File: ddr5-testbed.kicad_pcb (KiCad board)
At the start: 6 copper layers, 69.6 x 30 mm, 64 parts, among them IC1 PCA6408APW, IC2 AT24CS01, J1 ddr4-sodimm-edge-connector, U1 MT60B2G8HB-48B_A, U2 TPS613221ADBVT

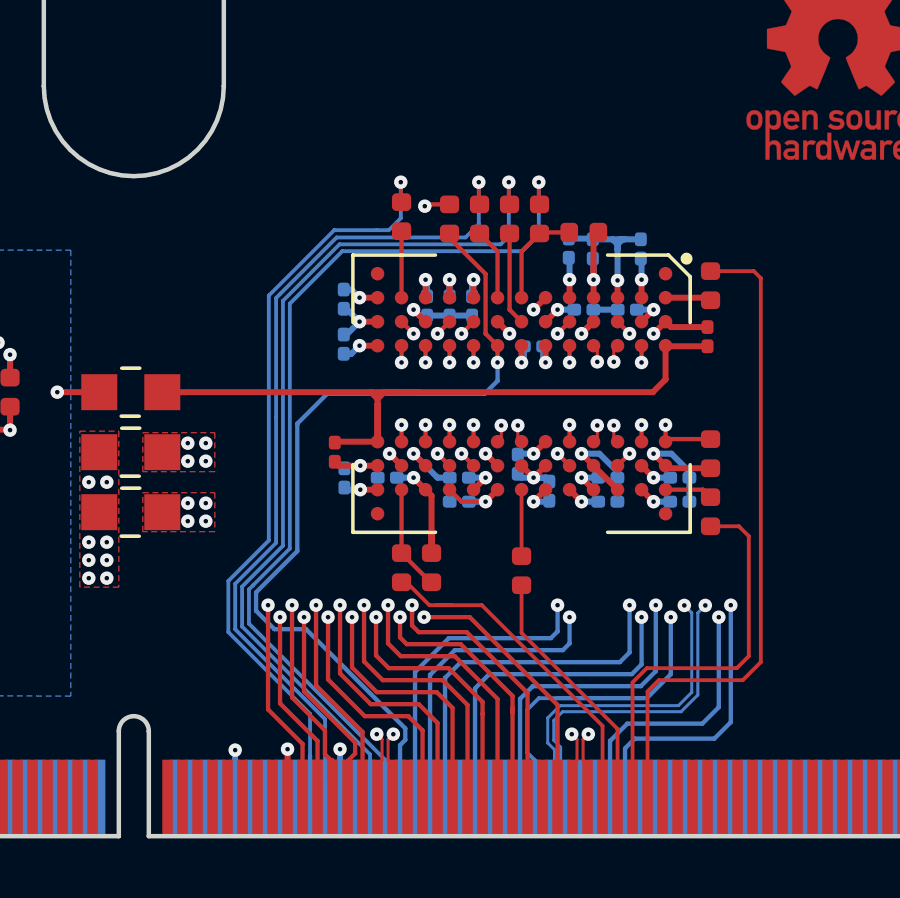
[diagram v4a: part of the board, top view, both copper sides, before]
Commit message: Finish SODIMM connections
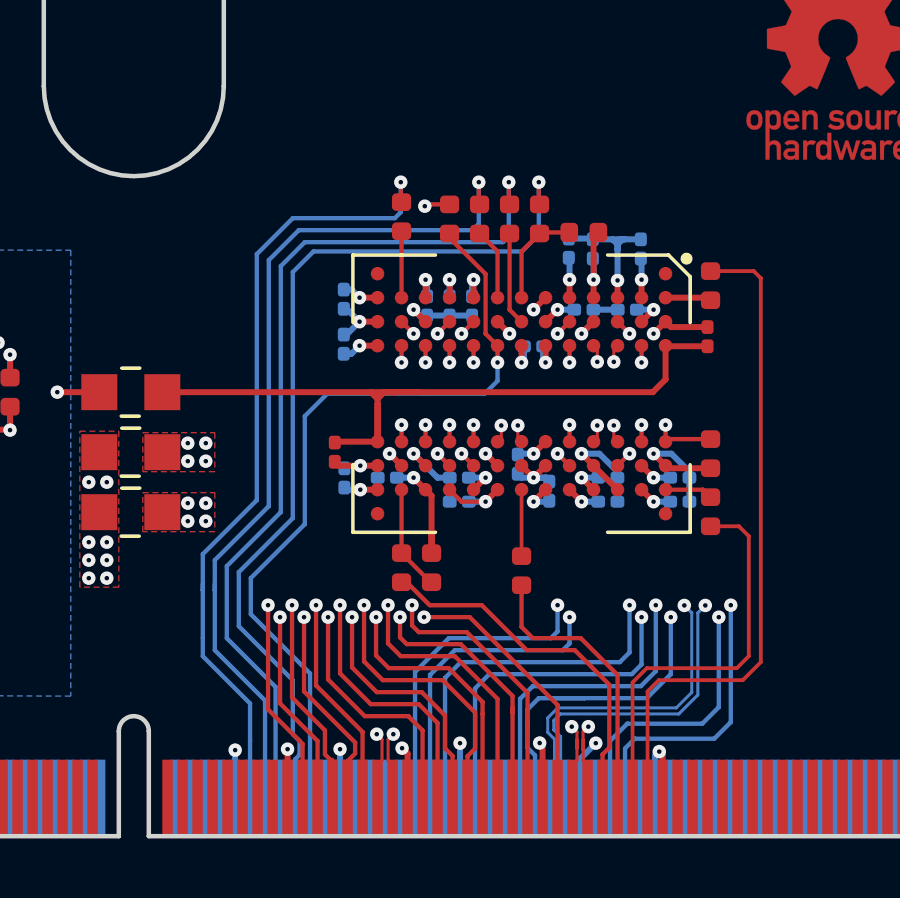
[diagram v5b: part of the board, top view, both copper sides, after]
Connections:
- J1 pad 156: (no net) -> CAI
- J1 pad 158: (no net) -> ALERT_N
- J1 pad 160: (no net) -> MIR
- J1 pad 162: (no net) -> OTD_CA_A
- J1 pad 164: CAI -> CS_N
- J1 pad 166: ALERT_N -> (no net)
- J1 pad 172: MIR -> (no net)
- J1 pad 174: OTD_CA_A -> (no net)
- J1 pad 176: CS_N -> (no net)
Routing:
- net GND: track 155.0 -> 165.5 mm, vias 56 -> 61
- net RESET_N: track 11.7 -> 15.7 mm
- net CS_N: track 28.6 -> 26.8 mm
- net DQ6: track 23.2 -> 24.9 mm
- net TEN: track 8.39 -> 9.33 mm
- net ALERT_N: track 28.4 -> 29.2 mm
- net OTD_CA_A: track 30.6 -> 31.2 mm

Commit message: Routing
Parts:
- R1, R15, R16, R2, R3, R4: moved to B.Cu
- moved R16 11.6 mm to (143.2, 88.2), turned to 225 degrees
- moved R15 9.39 mm to (142.4, 87.4), turned to 225 degrees
- moved R4 8.82 mm to (144.3, 86.3), turned to 225 degrees
- moved R2 7.99 mm to (156.9, 85.6), turned to 0 degrees
- moved R3 6.32 mm to (151.4, 85.2), turned to 0 degrees
- moved R1 5.94 mm to (156.9, 84.6)
- moved R5 2.00 mm to (150.2, 91.2)
- moved R7 2.00 mm to (149.2, 91.2)
- moved C7 1.78 mm to (148.0, 80.5), turned to 90 degrees
- moved C11 1.78 mm to (149.6, 80.5), turned to 90 degrees
- moved C9 1.78 mm to (148.8, 80.5), turned to 90 degrees
- moved C10 1.68 mm to (152.4, 88.0), turned to 180 degrees
- moved C23 1.67 mm to (152.4, 88.8), turned to 180 degrees
- moved C2 1.59 mm to (150.8, 87.6), turned to 180 degrees
- moved C14 0.78 mm to (150.8, 86.9), turned to 180 degrees
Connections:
- net Net-(R1-Pad2) renamed /DDR5/R_ODT_CA_A
- net Net-(R15-Pad1) renamed /DDR5/R_CAI
- net Net-(R16-Pad1) renamed /DDR5/R_MIR
- net Net-(R17-Pad1) renamed /DDR5/R_TEN
- net Net-(R18-Pad1) renamed /DDR5/R_LBDQ
- net Net-(R19-Pad1) renamed /DDR5/R_LBDQS
- net Net-(R4-Pad1) renamed /DDR5/R_ALERT_N
- net Net-(R5-Pad2) renamed /DDR5/R_RESET_N
- net Net-(R6-Pad1) renamed /DDR5/ZQ
- J1 pad 162: OTD_CA_A -> CS_N
- J1 pad 164: CS_N -> TDQS_N
- J1 pad 166: (no net) -> TDQS_P
- J1 pad 178: DQ5 -> DQ6
- J1 pad 180: DQ7 -> DQ5
- J1 pad 182: DQ1 -> DQ7
- J1 pad 186: DQ3 -> DQ4
- J1 pad 192: DQ4 -> DQ1
- J1 pad 194: DQ6 -> DQ3
- J1 pad 196: DQS_N -> DQ2
- J1 pad 198: DQS_P -> DQ0
- J1 pad 199: TDQS_N -> DQS_N
- J1 pad 201: TDQS_P -> DQS_P
- J1 pad 204: DQ2 -> (no net)
- J1 pad 206: DQ0 -> OTD_CA_A
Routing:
- net MIR: track 29.7 -> 11.0 mm, vias 1 -> 0
- net OTD_CA_A: track 31.2 -> 14.3 mm, vias 1 -> 0
- net ALERT_N: track 29.2 -> 13.5 mm, vias 1 -> 0
- net CAI: track 26.8 -> 11.7 mm, vias 1 -> 0
- net /DDR5/R_MIR: track 3.11 -> 11.2 mm, vias 0 -> 1
- net DQ6: track 24.9 -> 17.3 mm
- net /DDR5/R_ALERT_N: track 2.39 -> 9.44 mm, vias 0 -> 1
- net DQ4: track 24.2 -> 18.3 mm
- net RESET_N: track 15.7 -> 10.1 mm
- net TDQS_N: track 13.8 -> 19.3 mm
- net /DDR5/R_CAI: track 2.22 -> 7.68 mm, vias 0 -> 1
- net TDQS_P: track 13.9 -> 19.3 mm
- net /DDR5/R_ODT_CA_A: track 3.39 -> 8.78 mm, vias 0 -> 1
- net DQS_N: track 23.0 -> 17.7 mm
- net CS_N: track 26.8 -> 21.6 mm
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
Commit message: Tune DQ traces
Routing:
- net DQ5: track 14.0 -> 20.4 mm
- net DQ1: track 14.2 -> 20.4 mm
- net DQ7: track 15.0 -> 20.4 mm
- net DQ3: track 15.4 -> 20.4 mm
- net DQ6: track 17.3 -> 20.4 mm
- net DQS_N: track 17.7 -> 20.4 mm
- net DQS_P: track 17.8 -> 20.4 mm
- net DQ4: track 18.3 -> 20.4 mm
- net DQ2: track 19.1 -> 21.0 mm
- net TDQS_N: track 19.3 -> 20.4 mm
- net TDQS_P: track 19.3 -> 20.4 mm
- net TEN: track 9.36 -> 10.0 mm

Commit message: Tune CA traces
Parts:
- moved R3 0.32 mm to (151.2, 85.0)
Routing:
- net CLK_P: track 14.8 -> 22.0 mm
- net CLK_N: track 14.8 -> 22.0 mm
- net CA11: track 15.0 -> 22.0 mm
- net CA7: track 15.0 -> 22.0 mm
- net CA5: track 15.7 -> 22.0 mm
- net CA9: track 15.9 -> 22.0 mm
- net CA3: track 16.0 -> 22.0 mm
- net CA1: track 16.6 -> 22.0 mm
- net CA13: track 15.9 -> 20.0 mm
- net VPP: track 25.7 -> 23.0 mm
- net CA8: track 19.7 -> 22.1 mm
- net CA2: track 19.8 -> 22.0 mm
- net /DDR5/R_ALERT_N: track 9.44 -> 7.65 mm
- net /DDR5/R_CAI: track 7.68 -> 9.45 mm
- net CA10: track 20.6 -> 22.1 mm
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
